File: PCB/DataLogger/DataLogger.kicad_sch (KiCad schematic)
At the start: 19 parts, among them J1 Power, U2 DS18B20, U3 DS18B20, U4 DS18B20, U5 SHT30-DIS

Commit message: Ordered Board
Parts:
- removed U2, U3, U4: DS18B20, ESP32Board:Screw Terminal 3*2.54 1WI, symbol Sensor_Temperature:DS18B20
- removed U5: SHT30-DIS, ESP32Board:Screw Terminal 4*2.54 SHT30, symbol Sensor_Humidity:SHT30-DIS
- added J10, J8, J9: Screw_Terminal_01x02, ESP32Board:Screw Terminal 2*2.54, symbol Connector:Screw_Terminal_01x02
- added J2, J3, J4: 1WI Screw_Terminal_01x03, ESP32Board:Screw Terminal 3*2.54 1WI, symbol ESP32Board:1WI Screw_Terminal_01x03
- added J5, J6: I²C_Screw_Terminal_01x04, ESP32Board:Screw Terminal 4*2.54 I²C, symbol ESP32Board:I²C_Screw_Terminal_01x04
- added J7: Screw_Terminal_01x04, ESP32Board:Screw Terminal 4*2.54, symbol Connector:Screw_Terminal_01x04
- added JP5, JP6, JP7, JP8, JP9: SolderJumper_3_Bridged12, Jumper:SolderJumper-3_P1.3mm_Bridged12_RoundedPad1.0x1.5mm_NumberLabels, symbol Jumper:SolderJumper_3_Bridged12
- added TP5: GPIO01, TestPoint:TestPoint_THTPad_D1.5mm_Drill0.7mm, symbol Connector:TestPoint
- added TP6: GPIO05, TestPoint:TestPoint_THTPad_D1.5mm_Drill0.7mm, symbol Connector:TestPoint
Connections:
- net +3V3: now also J9.1 (Pin_1)
- net +5V: now also J8.1 (Pin_1)
- net GND: now also J2.1 (GND), J3.1 (GND), J4.1 (GND), J5.3 (GND), J6.3 (GND), J8.2 (Pin_2), J9.2 (Pin_2), JP5.3 (B), JP6.3 (B), JP7.3 (B), JP8.3 (B), JP9.3 (B)
- net at R2.1: now also JP6.2 (C); no longer U1.27 (16)
- net at JP2.2 (C): now also J3.3 (VDD), JP6.1 (A); no longer R2.2
- net at JP1.2 (C): now also J2.3 (VDD), JP5.1 (A); no longer R1.2
- net at R9.1, U1.36 (22): now also J5.2 (SCL), J6.2 (SCL)
- net at R3.1: now also JP7.2 (C); no longer U1.23 (15)
- net at R3.2: now also U1.30 (18), J4.2 (Data); no longer JP3.2 (C)
- net at R1.1, U1.28 (17): now also J2.2 (Data)
- net at R10.2, U1.33 (21): now also J5.1 (SDA), J6.1 (SDA)
- net at U1.10 (26): now also J10.2 (Pin_2)
- net at U1.24 (2): now also J7.3 (Pin_3)
- net at U1.25 (0): now also J7.2 (Pin_2)
- net at U1.26 (4): now also J7.1 (Pin_1)
- net at U1.29 (5): now also TP6.1
- net at U1.35 (1): now also TP5.1
- net at U1.9 (25): now also J10.1 (Pin_1)
- new net: J4.3 (VDD), JP3.2 (C), JP7.1 (A)
- new net: J5.4 (VDD), J6.4 (VDD), JP4.2 (C), JP8.1 (A), JP9.1 (A)
- new net: JP9.2 (C), R10.1
- new net: JP5.2 (C), R1.2
- new net: JP8.2 (C), R9.2
- new net: J3.2 (Data), R2.2, U1.27 (16)
- new net: J7.4 (Pin_4), U1.23 (15)
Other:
- moved on the sheet: R2, R3

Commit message: PCB V1.2
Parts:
- removed J4: 1WI Screw_Terminal_01x03, ESP32Board:Screw Terminal 3*2.54 1WI, symbol ESP32Board:1WI Screw_Terminal_01x03
- added 1WI3: 1WI Screw_Terminal_01x03, ESP32Board:Screw Terminal 3*2.54 1WI, symbol ESP32Board:1WI Screw_Terminal_01x03
- added R4: 4k7, Resistor_THT:R_Axial_DIN0207_L6.3mm_D2.5mm_P7.62mm_Horizontal, symbol Device:R
- added U2: DS18B20, Package_TO_SOT_THT:TO-92_Inline, symbol Sensor_Temperature:DS18B20
- ExtraGPIO2: renamed from J10; value Screw_Terminal_01x02 -> Screw_Terminal_01x
- R1, R10, R2, R3, R9: value 1k5 -> 2k2
- TP5: value GPIO01 -> 01
- TP6: value GPIO05 -> 05
- renumbered J2 to 1WI1, J3 to 1WI2, J7 to ExtraGPIO1, J5 to I²C1, J6 to I²C2, J1 to Power1
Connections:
- net +3V3: now also R4.2, U2.3 (V_{DD})
- net GND: now also 1WI3.1 (GND), U2.1 (GND)
- net RESET: now reaches TP4.1, U1.2 (RESET)
- net IO18: now reaches R3.2, U1.30 (18)
- net IO18: now also 1WI3.2 (Data)
- net at JP3.2 (C), JP7.1 (A): now also 1WI3.3 (VDD)
- net IO17: now reaches 1WI1.2 (Data), R1.1, U1.28 (17)
- net IO25: now reaches ExtraGPIO2.1 (Pin_1), U1.9 (25)
- net IO26: now reaches ExtraGPIO2.2 (Pin_2), U1.10 (26)
- net IO16: now reaches 1WI2.2 (Data), R2.2, U1.27 (16)
- net IO00: now reaches ExtraGPIO1.1 (Pin_1)
- net IO00: now also U1.25 (0); no longer U1.26 (4)
- net IO02: now reaches ExtraGPIO1.2 (Pin_2)
- net IO02: now also U1.24 (2); no longer U1.25 (0)
- net IO04: now reaches ExtraGPIO1.3 (Pin_3)
- net IO04: now also U1.26 (4); no longer U1.24 (2)
- net IO15: now reaches ExtraGPIO1.4 (Pin_4), U1.23 (15)
- net IO05: now reaches TP6.1, U1.29 (5)
- net IO01: now reaches TP5.1, U1.35 (1)
- net IO13: now reaches U1.15 (13)
- net IO13: now also R4.1, U2.2 (DQ)
- no-connect marks 0 -> 18

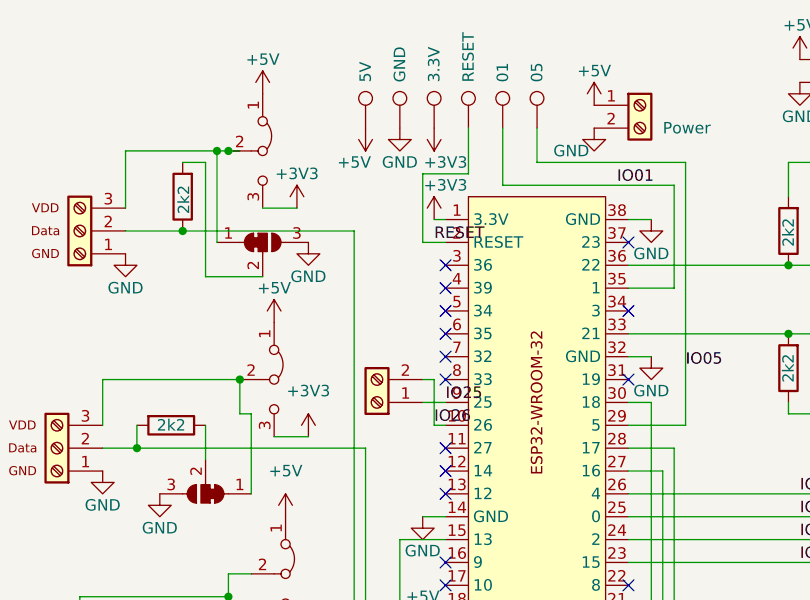
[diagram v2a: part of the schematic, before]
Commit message: Add voltage devider to measure supply voltage
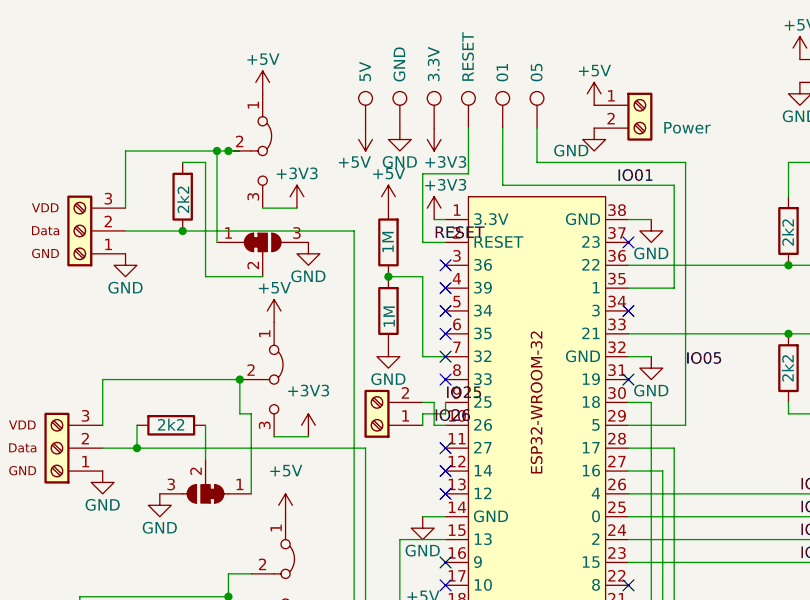
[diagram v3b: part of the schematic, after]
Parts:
- added R5, R6: 1M, Resistor_THT:R_Axial_DIN0207_L6.3mm_D2.5mm_P7.62mm_Horizontal, symbol Device:R
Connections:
- net +5V: now also R5.2
- net GND: now also R6.1
- net at U1.7 (32): now also R5.1, R6.2
